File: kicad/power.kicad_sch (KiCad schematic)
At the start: 63 parts, among them J50 VIN 12V, U11 TPS54202DDC, U12 TLV62569DRL, U13 TLV62569DRL, U14 TLV62569DRL, U15 TLV62569DRL, U16 TLV62569DRL

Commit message: power input: single USB-C with CH224K PD sink at 9V, Schottky OR-ing, degraded 5V mode; record missing board-ID pins
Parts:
- removed C150: 22uF, Capacitor_SMD:C_0805_2012Metric, symbol Device:C
- removed R61: 1k, Resistor_SMD:R_0603_1608Metric, symbol Device:R
- removed R62, R63, R64, R65: 10k, Resistor_SMD:R_0402_1005Metric, symbol Device:R
- added C173: 4.7uF, Capacitor_SMD:C_0603_1608Metric, symbol Device:C
- added D3, D4: SS34, Diode_SMD:D_SMA, symbol Device:D_Schottky
- added R40: 100k, Resistor_SMD:R_0603_1608Metric, symbol Device:R
- C152: value 10uF -> 22uF
- C153: value 100nF -> 10uF; footprint Capacitor_SMD:C_0402_1005Metric -> Capacitor_SMD:C_0805_2012Metric
- C154, C160, C163, C166, C169: value 22uF -> 100nF; footprint Capacitor_SMD:C_0805_2012Metric -> Capacitor_SMD:C_0402_1005Metric
- C159, C162, C165, C168, C171: value 100nF -> 22uF; footprint Capacitor_SMD:C_0402_1005Metric -> Capacitor_SMD:C_0805_2012Metric
- C172: value 4.7uF -> 100nF; footprint Capacitor_SMD:C_0603_1608Metric -> Capacitor_SMD:C_0402_1005Metric
- J50: value VIN 12V -> VIN (optional)
- R41: value 100k -> 13.7k
- R42: value 13.7k -> 100k
- R43: value 100k -> 22.1k
- R44: value 22.1k -> 100k
- R45: value 100k -> 31.6k
- R46: value 31.6k -> 100k
- R47: value 100k -> 49.9k
- R48: value 49.9k -> 100k
- R49: value 100k -> 150k
- R50: value 150k -> 100k
- R53: value 100k -> 33k
- R54: value 33k -> 100k
- R56: value 100k -> 1k
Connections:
- net +1V0: now also C168.1, R48.1, R59.1; no longer C166.1, R49.1, R60.1
- net +1V0_MGT: now also C173.1; no longer C172.1
- net +1V2_MGT: now also C171.1, R50.1, R60.1; no longer C169.1, R51.1
- net +1V8: now also C165.1, R46.1, R58.1; no longer C163.1, R47.1, R59.1
- net +2V5: now also C162.1, R44.1, R57.1; no longer C160.1, R45.1, R58.1
- net +3V3: now also C159.1, R42.1, R56.1; no longer C157.1, R43.1, R57.1
- net +5V: now also C157.1, C160.1, C163.1, C166.1, C169.1, C172.1, R54.1, R40.1; no longer C154.1, C159.1, C162.1, C165.1, C168.1, C171.1, R41.1, R55.1
- net BOOT_5V: now also C154.1; no longer C153.1
- net FB+1V0: now also R48.2, R49.1; no longer R49.2, R50.1
- net FB+1V2_MGT: now also R50.2, R51.1; no longer R51.2, R52.1
- net FB+1V8: now also R46.2, R47.1; no longer R47.2, R48.1
- net FB+2V5: now also R44.2, R45.1; no longer R45.2, R46.1
- net FB+3V3: now also R42.2, R43.1; no longer R43.2, R44.1
- net FB_5V: now also R41.1, R40.2; no longer R41.2, R42.1
- net GND: now also C153.2, R41.2, R43.2, R45.2, R47.2, R49.2, R51.2, R53.2, R55.2, C173.2; no longer C154.2, R42.2, R44.2, R46.2, R48.2, R50.2, R52.2, R54.2, R56.2
- net MON_1V0: now also R59.2; no longer R60.2
- net MON_1V2: now also R60.2
- net MON_1V8: now also R58.2; no longer R59.2
- net MON_2V5: now also R57.2; no longer R58.2
- net MON_3V3: now also R56.2; no longer R57.2
- net MON_5V: now also R54.2, R55.1; no longer R55.2, R56.1
- net SW_5V: now also C154.2; no longer C153.2
- net VBUS: now also C153.1, D3.2 (A); no longer C152.1
- net +12V renamed VSYS
- net VSYS: now also C152.1, R52.1, D3.1 (K), D4.1 (K); no longer J50.1 (Pin_1), R53.1
- removed net MON_12V: R53.2, R54.1
- new net MON_VSYS: R52.2, R53.1
- new net VIN_EXT: D4.2 (A), J50.1 (Pin_1)
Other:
- note added: "input OR-ing"
- note removed: "12V input"
- note removed: "board-ID pull-downs"
- moved on the sheet: C151, C152, C153, C154, C155, C156, C157, C158, C159, C160, C161, C162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

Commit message: assume 5V for function, PD only for headroom: boost 12V AUX from the 5V rail
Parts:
- added C174: 10nF, Capacitor_SMD:C_0402_1005Metric, symbol Device:C
- added C175, C176, C177: 10uF, Capacitor_SMD:C_0805_2012Metric, symbol Device:C
- added C178: 4.7uF, Capacitor_SMD:C_0603_1608Metric, symbol Device:C
- added D5: SS34, Diode_SMD:D_SMA, symbol Device:D_Schottky
- added L9: 1uH, Inductor_SMD:L_Bourns-SRN4018, symbol Device:L
- added R61, R62: 1k, Resistor_SMD:R_0603_1608Metric, symbol Device:R
- added U19: TPS61085PW, Package_SO:TSSOP-8_3x3mm_P0.65mm, symbol Regulator_Switching:TPS61085PW
- C173: value 4.7uF -> 2.2nF; footprint Capacitor_SMD:C_0603_1608Metric -> Capacitor_SMD:C_0402_1005Metric
- L8: value 1uH -> 4.7uH
- R53: value 33k -> 11.5k
- R54: value 100k -> 47k; footprint Resistor_SMD:R_0603_1608Metric -> Resistor_SMD:R_0402_1005Metric
- R56: value 1k -> 33k
- R57, R58: value 1k -> 100k
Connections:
- net MON_1V2 is gone; now on net MON_2V5: R60.2
- net +1V0: now also L9.2, R62.1; no longer L8.2, R59.1
- net +1V0_MGT: now also C178.1, L9.1; no longer C173.1, L8.1
- net +1V2_MGT: no longer R60.1
- net +1V8: now also R61.1; no longer R58.1
- net +2V5: now also R60.1; no longer R57.1
- net +3V3: now also R59.1; no longer R56.1
- net +5V: now also L8.1, R57.1, C177.1, U19.6 (VIN); no longer R54.1
- net GND: now also R56.2, R58.2, C174.2, C175.2, C176.2, C177.2, C178.2, U19.4 (GND), U19.7 (FREQ); no longer R55.2
- net MON_1V0: now also R62.2; no longer R59.2
- net MON_1V8: now also R61.2; no longer R58.2
- net MON_2V5: no longer R57.2
- net MON_3V3: now also R59.2; no longer R56.2
- net MON_5V: now also R57.2, R58.1; no longer R54.2, R55.1
- net MON_VSYS: now also R55.2, R56.1; no longer R52.2, R53.1
- net VSYS: now also R55.1; no longer R52.1
- new net +12V: C175.1, C176.1, D5.1 (K), R52.1
- new net COMP_12V: R54.1, U19.1 (COMP)
- new net COMP_12V_C: C173.1, R54.2
- new net EN_12V: U19.3 (EN)
- new net FB_12V: R52.2, R53.1, U19.2 (FB)
- new net SS_12V: C174.1, U19.8 (SS)
- new net SW_12V: D5.2 (A), L8.2, U19.5 (SW)
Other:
- note added: "U19 5V to 12V boost (AUX)"
- moved on the sheet: C158, C159, C160, C161, C162, C163, C164, C165, C166, C167, C168, C169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

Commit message: supervisor flash: document the role, add BOOTSEL series resistor
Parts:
- removed R40: 100k, Resistor_SMD:R_0603_1608Metric, symbol Device:R
- added R63: 1k, Resistor_SMD:R_0603_1608Metric, symbol Device:R
- R41: value 13.7k -> 100k
- R42: value 100k -> 13.7k
- R43: value 22.1k -> 100k
- R44: value 100k -> 22.1k
- R45: value 31.6k -> 100k
- R46: value 100k -> 31.6k
- R47: value 49.9k -> 100k
- R48: value 100k -> 49.9k
- R49: value 150k -> 100k
- R50: value 100k -> 150k
- R53: value 11.5k -> 100k
- R54: value 47k -> 11.5k; footprint Resistor_SMD:R_0402_1005Metric -> Resistor_SMD:R_0603_1608Metric
- R55: value 100k -> 47k; footprint Resistor_SMD:R_0603_1608Metric -> Resistor_SMD:R_0402_1005Metric
- R56: value 33k -> 100k
- R57: value 100k -> 33k
- R59: value 1k -> 100k
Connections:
- net +12V: now also R53.1; no longer R52.1
- net +1V0: now also R49.1, R63.1; no longer R48.1, R62.1
- net +1V2_MGT: now also R51.1; no longer R50.1
- net +1V8: now also R47.1, R62.1; no longer R46.1, R61.1
- net +2V5: now also R45.1, R61.1; no longer R44.1, R60.1
- net +3V3: now also R43.1, R60.1; no longer R42.1, R59.1
- net +5V: now also R41.1, R58.1; no longer R57.1
- net COMP_12V: now also R55.1; no longer R54.1
- net COMP_12V_C: now also R55.2; no longer R54.2
- net FB+1V0: now also R49.2, R50.1; no longer R48.2, R49.1
- net FB+1V2_MGT: now also R51.2, R52.1; no longer R50.2, R51.1
- net FB+1V8: now also R47.2, R48.1; no longer R46.2, R47.1
- net FB+2V5: now also R45.2, R46.1; no longer R44.2, R45.1
- net FB+3V3: now also R43.2, R44.1; no longer R42.2, R43.1
- net FB_12V: now also R53.2, R54.1; no longer R52.2, R53.1
- net FB_5V: now also R41.2, R42.1; no longer R41.1
- net GND: now also R42.2, R44.2, R46.2, R48.2, R50.2, R52.2, R54.2, R57.2, R59.2; no longer R41.2, R43.2, R45.2, R47.2, R49.2, R51.2, R53.2, R56.2, R58.2
- net MON_1V0: now also R63.2; no longer R62.2
- net MON_1V8: now also R62.2; no longer R61.2
- net MON_2V5: now also R61.2; no longer R60.2
- net MON_3V3: now also R60.2; no longer R59.2
- net MON_5V: now also R58.2, R59.1; no longer R57.2, R58.1
- net MON_VSYS: now also R56.2, R57.1; no longer R55.2, R56.1
- net VSYS: now also R56.1; no longer R55.1
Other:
- moved on the sheet: R41, R42, R43, R44, R45, R46, R47, R48, R49, R50, R51, R52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

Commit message: fix boot deadlock (+3V3 now always-on off VSYS) and VBUS overvoltage hazard (switch, not diode)
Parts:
- removed D2: SS34, Diode_SMD:D_SMA, symbol Device:D_Schottky
- added C179: 4.7uF, Capacitor_SMD:C_0603_1608Metric, symbol Device:C
- added Q2: VBUS pass, Package_TO_SOT_SMD:SOT-23, symbol Device:Q_PMOS
- added Q3: gate driver, Package_TO_SOT_SMD:SOT-23, symbol Device:Q_NMOS
- added R64, R65, R66, R67: 1k, Resistor_SMD:R_0603_1608Metric, symbol Device:R
- C158, C164, C167, C170: value 22uF -> 100nF; footprint Capacitor_SMD:C_0805_2012Metric -> Capacitor_SMD:C_0402_1005Metric
- C160, C163, C166, C169, C172: value 100nF -> 22uF; footprint Capacitor_SMD:C_0402_1005Metric -> Capacitor_SMD:C_0805_2012Metric
- C173: value 2.2nF -> 100nF
- C174: value 10nF -> 2.2nF
- C175: value 10uF -> 10nF; footprint Capacitor_SMD:C_0805_2012Metric -> Capacitor_SMD:C_0402_1005Metric
- C178: value 4.7uF -> 10uF; footprint Capacitor_SMD:C_0603_1608Metric -> Capacitor_SMD:C_0805_2012Metric
- L3: value 1.5uH -> 4.7uH
- R42: value 13.7k -> 10k; footprint Resistor_SMD:R_0603_1608Metric -> Resistor_SMD:R_0402_1005Metric
- R43: footprint Resistor_SMD:R_0603_1608Metric -> Resistor_SMD:R_0402_1005Metric
- R44: value 22.1k -> 100k
- R45: value 100k -> 13.7k
- R46: value 31.6k -> 100k
- R48: value 49.9k -> 22.1k
- R50: value 150k -> 31.6k
- R52: value 100k -> 49.9k
- R54: value 11.5k -> 150k
- R55: value 47k -> 100k; footprint Resistor_SMD:R_0402_1005Metric -> Resistor_SMD:R_0603_1608Metric
- R57: value 33k -> 100k
- R58: value 100k -> 11.5k
- R59: value 100k -> 47k; footprint Resistor_SMD:R_0603_1608Metric -> Resistor_SMD:R_0402_1005Metric
- R60, R62, R63: value 1k -> 100k
- R61: value 1k -> 33k
- U12: value TLV62569DRL -> TPS54202DDC; symbol Regulator_Switching:TLV62569DRL -> Regulator_Switching:TPS54202DDC; LCSC C163217 -> C191884
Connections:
- net +12V: now also C177.1, R57.1; no longer C175.1, R53.1
- net +1V0: now also C169.1, R53.1, R67.1; no longer C167.1, R49.1, R63.1
- net +1V0_MGT: now also C179.1; no longer C178.1
- net +1V2_MGT: now also C172.1, R55.1; no longer C170.1, R51.1
- net +1V8: now also C166.1, R51.1, R66.1; no longer C164.1, R47.1, R62.1
- net +2V5: now also C163.1, R49.1, R65.1; no longer C161.1, R45.1, R61.1
- net +3V3: now also C160.1, C161.1, R47.1, R64.1; no longer C158.1, R43.1, R60.1
- net +5V: now also C164.1, C167.1, C170.1, C173.1, C178.1, R44.1, R62.1, Q2.D; no longer C160.1, C163.1, C166.1, C169.1, C172.1, C177.1, R41.1, R58.1, U12.3 (VIN)
- net COMP_12V: now also R59.1; no longer R55.1
- net COMP_12V_C: now also C174.1, R59.2; no longer C173.1, R55.2
- net FB+1V0: now also R53.2, R54.1; no longer R49.2, R50.1
- net FB+1V2_MGT: now also R55.2, R56.1; no longer R51.2, R52.1
- net FB+1V8: now also R51.2, R52.1; no longer R47.2, R48.1
- net FB+2V5: now also R49.2, R50.1; no longer R45.2, R46.1
- net FB_12V: now also R57.2, R58.1; no longer R53.2, R54.1
- net FB_5V: now also R44.2, R45.1; no longer R41.2, R42.1
- net GND: now also R43.2, R45.2, R56.2, R58.2, R61.2, R63.2, U12.1 (GND), C179.2, Q3.S; no longer C158.2, R42.2, R44.2, R46.2, R57.2, R59.2, U12.2 (GND)
- net MON_1V0: now also R67.2; no longer R63.2
- net MON_1V8: now also R66.2; no longer R62.2
- net MON_2V5: now also R65.2; no longer R61.2
- net MON_3V3: now also R64.2; no longer R60.2
- net MON_5V: now also R62.2, R63.1; no longer R58.2, R59.1
- net MON_VSYS: now also R60.2, R61.1; no longer R56.2, R57.1
- net SS_12V: now also C175.1; no longer C174.1
- net VBUS: now also R41.1, Q2.S
- net VSYS: now also R46.1, R60.1, U12.3 (VIN); no longer R56.1
- net BOOT_3V3: now reaches U12.6 (BOOT)
- net BOOT_3V3: now also C158.1
- net EN_3V3 renamed EN_3V3_AO
- net EN_3V3_AO: now also R46.2
- removed net FB+3V3: R43.2, R44.1, U12.1 (FB)
- net SW+3V3 renamed FB_3V3
- net FB_3V3: now also R47.2, R48.1; no longer L3.2
- new net EN_VBUS5: R42.1
- new net EN_VBUS5_G: Q3.G, R42.2, R43.1
- new net SW_3V3: C158.2, L3.2, U12.2 (SW)
- new net VBUS5_GATE: Q2.G, Q3.D, R41.2
- no-connect marks 5 -> 4
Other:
- note added: "U12 VSYS to +3V3 (always on)"
- note added: "VBUS pass switch to +5V"
- note removed: "U12 5V to +3V3"
- moved on the sheet: C151, C152, C153, C154, C155, C156, C157, C158, C159, C160, C161, C162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

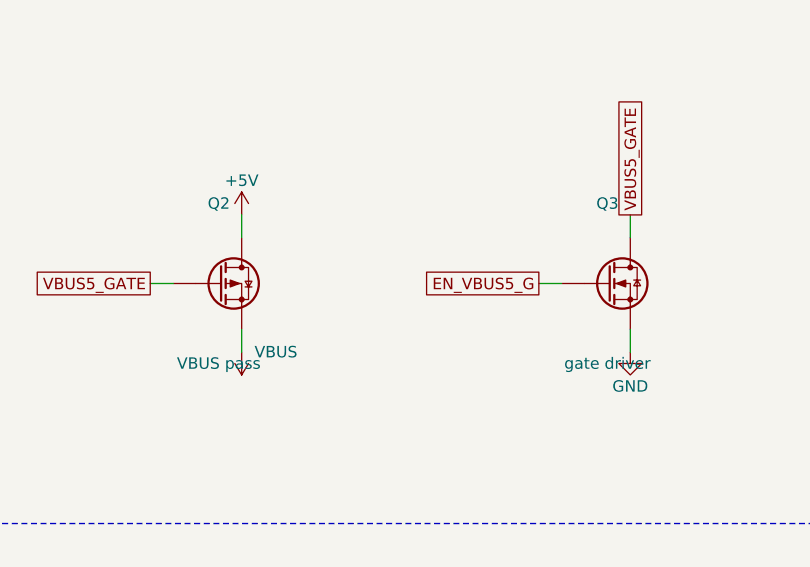
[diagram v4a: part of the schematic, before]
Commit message: audit response: fix 5V-overstressed translators, add USB ESD protection and keying posts, load the PCB, reconcile every stale doc
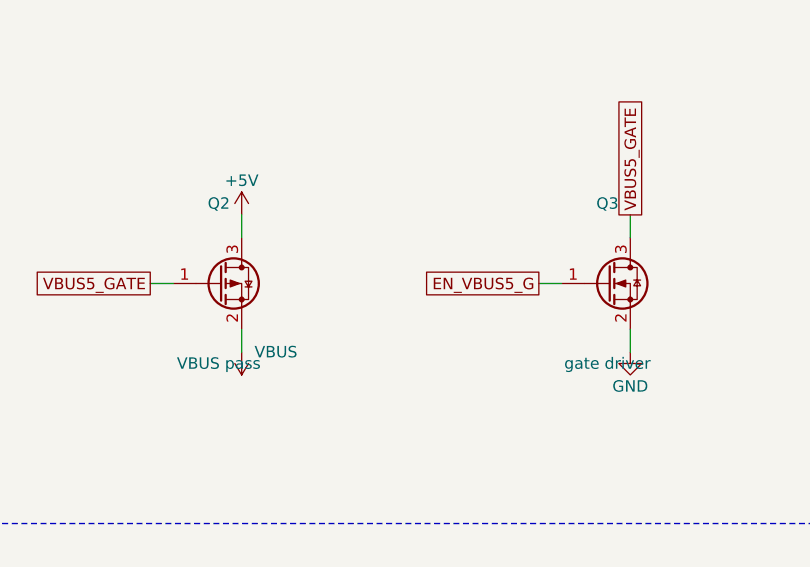
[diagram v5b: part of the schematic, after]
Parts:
- Q2: symbol Device:Q_PMOS -> Transistor_FET:Q_PMOS_GSD
- Q3: symbol Device:Q_NMOS -> Transistor_FET:Q_NMOS_GSD
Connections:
- net +5V: now also Q2.3 (D); no longer Q2.D
- net EN_VBUS5_G: now also Q3.1 (G); no longer Q3.G
- net GND: now also Q3.2 (S); no longer Q3.S
- net VBUS: now also Q2.2 (S); no longer Q2.S
- net VBUS5_GATE: now also Q2.1 (G), Q3.3 (D); no longer Q2.G, Q3.D
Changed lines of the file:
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@@
 	(wire (pts (xy 121.92 76.2) (xy 121.92 78.74)) (stroke (width 0) (type default)))
 	(global_label "EN_VBUS5_G" (shape passive) (at 121.92 78.74 90) (fields_autoplaced yes) (effects (font (size 1.27 1.27)) (justify right)))
-	(symbol (lib_id "Device:Q_PMOS") (at 160.02 73.66 0) (unit 1)
+	(symbol (lib_id "Transistor_FET:Q_PMOS_GSD") (at 160.02 73.66 0) (unit 1)
 		(exclude_from_sim no) (in_bom yes) (on_board yes) (dnp no)
 		(property "Reference" "Q2" (at 160.02 64.77 0) (effects (font (size 1.27 1.27))))
@@
 		(instances (project "odin" (path "/c44fb7fe-6133-ad34-68fd-fb66126197ef/d8079187-14d6-b109-30bb-e1c878749fb7" (reference "#PWR0299") (unit 1))))
 	)
-	(symbol (lib_id "Device:Q_NMOS") (at 203.2 73.66 0) (unit 1)
+	(symbol (lib_id "Transistor_FET:Q_NMOS_GSD") (at 203.2 73.66 0) (unit 1)
 		(exclude_from_sim no) (in_bom yes) (on_board yes) (dnp no)
 		(property "Reference" "Q3" (at 203.2 64.77 0) (effects (font (size 1.27 1.27))))

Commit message: fix 14 package mismatches, assert footprints against ki_fp_filters, rebalance fuses, correct JTAG and PD-voltage claims
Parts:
- U13, U14, U15, U16: footprint Package_TO_SOT_SMD:SOT-23-6 -> Package_TO_SOT_SMD:SOT-563
- U19: footprint Package_SO:TSSOP-8_3x3mm_P0.65mm -> Package_SO:TSSOP-8_4.4x3mm_P0.65mm
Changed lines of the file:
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@@
 		(property "Reference" "U13" (at 378.46 278.13 0) (effects (font (size 1.27 1.27))))
 		(property "Value" "TLV62569DRL" (at 378.46 300.99 0) (effects (font (size 1.27 1.27))))
-		(property "Footprint" "Package_TO_SOT_SMD:SOT-23-6" (at 378.46 300.99 0) (effects (font (size 1.27 1.27)) (hide yes)))
+		(property "Footprint" "Package_TO_SOT_SMD:SOT-563" (at 378.46 300.99 0) (effects (font (size 1.27 1.27)) (hide yes)))
 		(property "LCSC" "C163217" (at 378.46 300.99 0) (effects (font (size 1.27 1.27)) (hide yes)))
 		(instances (project "odin" (path "/c44fb7fe-6133-ad34-68fd-fb66126197ef/d8079187-14d6-b109-30bb-e1c878749fb7" (reference "U13") (unit 1))))
@@
 		(property "Reference" "U14" (at 85.09 411.48 0) (effects (font (size 1.27 1.27))))
 		(property "Value" "TLV62569DRL" (at 85.09 434.34 0) (effects (font (size 1.27 1.27))))
-		(property "Footprint" "Package_TO_SOT_SMD:SOT-23-6" (at 85.09 434.34 0) (effects (font (size 1.27 1.27)) (hide yes)))
+		(property "Footprint" "Package_TO_SOT_SMD:SOT-563" (at 85.09 434.34 0) (effects (font (size 1.27 1.27)) (hide yes)))
 		(property "LCSC" "C163217" (at 85.09 434.34 0) (effects (font (size 1.27 1.27)) (hide yes)))
 		(instances (project "odin" (path "/c44fb7fe-6133-ad34-68fd-fb66126197ef/d8079187-14d6-b109-30bb-e1c878749fb7" (reference "U14") (unit 1))))
@@
 		(property "Reference" "U15" (at 312.42 411.48 0) (effects (font (size 1.27 1.27))))
 		(property "Value" "TLV62569DRL" (at 312.42 434.34 0) (effects (font (size 1.27 1.27))))
-		(property "Footprint" "Package_TO_SOT_SMD:SOT-23-6" (at 312.42 434.34 0) (effects (font (size 1.27 1.27)) (hide yes)))
+		(property "Footprint" "Package_TO_SOT_SMD:SOT-563" (at 312.42 434.34 0) (effects (font (size 1.27 1.27)) (hide yes)))
 		(property "LCSC" "C163217" (at 312.42 434.34 0) (effects (font (size 1.27 1.27)) (hide yes)))
 		(instances (project "odin" (path "/c44fb7fe-6133-ad34-68fd-fb66126197ef/d8079187-14d6-b109-30bb-e1c878749fb7" (reference "U15") (unit 1))))
@@
 		(property "Reference" "U16" (at 85.09 543.56 0) (effects (font (size 1.27 1.27))))
 		(property "Value" "TLV62569DRL" (at 85.09 566.42 0) (effects (font (size 1.27 1.27))))
-		(property "Footprint" "Package_TO_SOT_SMD:SOT-23-6" (at 85.09 566.42 0) (effects (font (size 1.27 1.27)) (hide yes)))
+		(property "Footprint" "Package_TO_SOT_SMD:SOT-563" (at 85.09 566.42 0) (effects (font (size 1.27 1.27)) (hide yes)))
 		(property "LCSC" "C163217" (at 85.09 566.42 0) (effects (font (size 1.27 1.27)) (hide yes)))
 		(instances (project "odin" (path "/c44fb7fe-6133-ad34-68fd-fb66126197ef/d8079187-14d6-b109-30bb-e1c878749fb7" (reference "U16") (unit 1))))
@@
 		(property "Reference" "U19" (at 87.63 676.91 0) (effects (font (size 1.27 1.27))))
 		(property "Value" "TPS61085PW" (at 87.63 704.85 0) (effects (font (size 1.27 1.27))))
-		(property "Footprint" "Package_SO:TSSOP-8_3x3mm_P0.65mm" (at 87.63 704.85 0) (effects (font (size 1.27 1.27)) (hide yes)))
+		(property "Footprint" "Package_SO:TSSOP-8_4.4x3mm_P0.65mm" (at 87.63 704.85 0) (effects (font (size 1.27 1.27)) (hide yes)))
 		(instances (project "odin" (path "/c44fb7fe-6133-ad34-68fd-fb66126197ef/d8079187-14d6-b109-30bb-e1c878749fb7" (reference "U19") (unit 1))))
 	)
